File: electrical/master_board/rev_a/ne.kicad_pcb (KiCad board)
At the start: 2 copper layers, 42.2 x 39 mm, 1 part, among them CN60 HCSR04H;F1X4

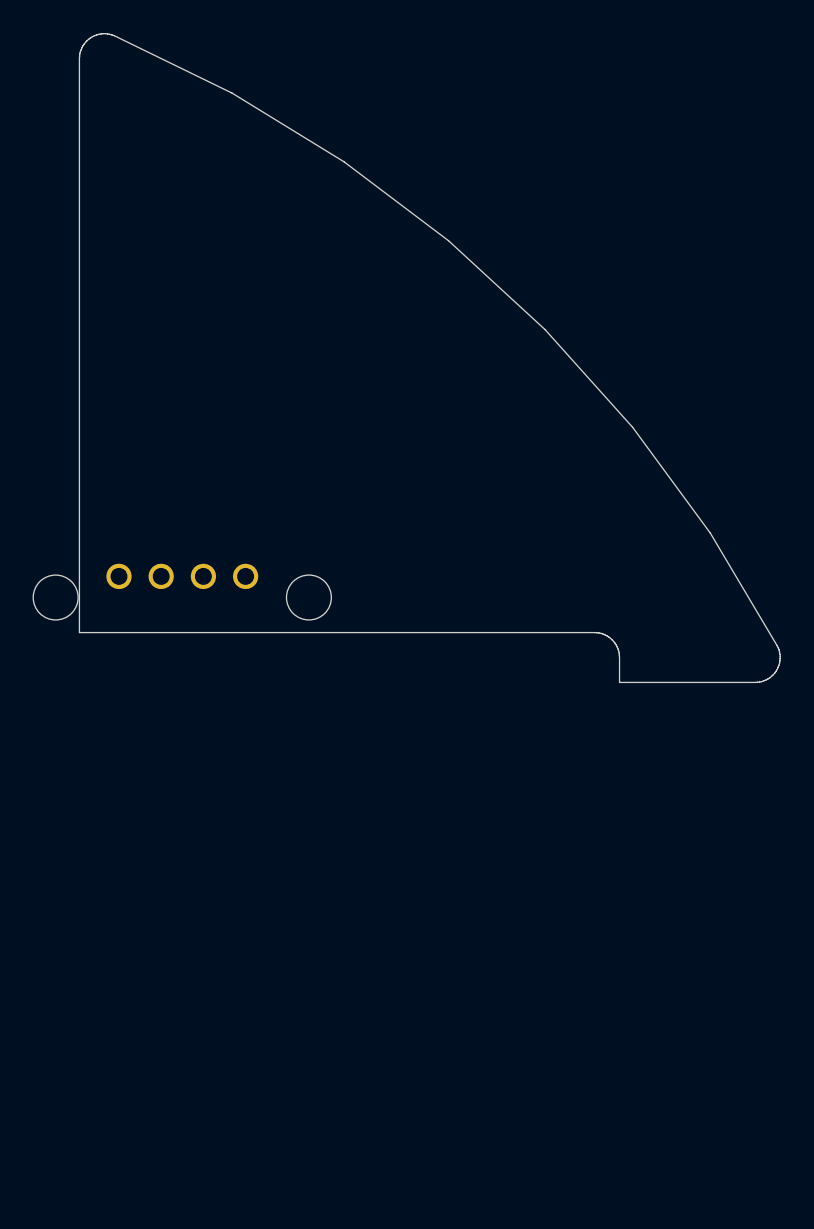
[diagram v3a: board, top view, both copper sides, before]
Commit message: Locked down a minimal version ne.kicad_pcb .
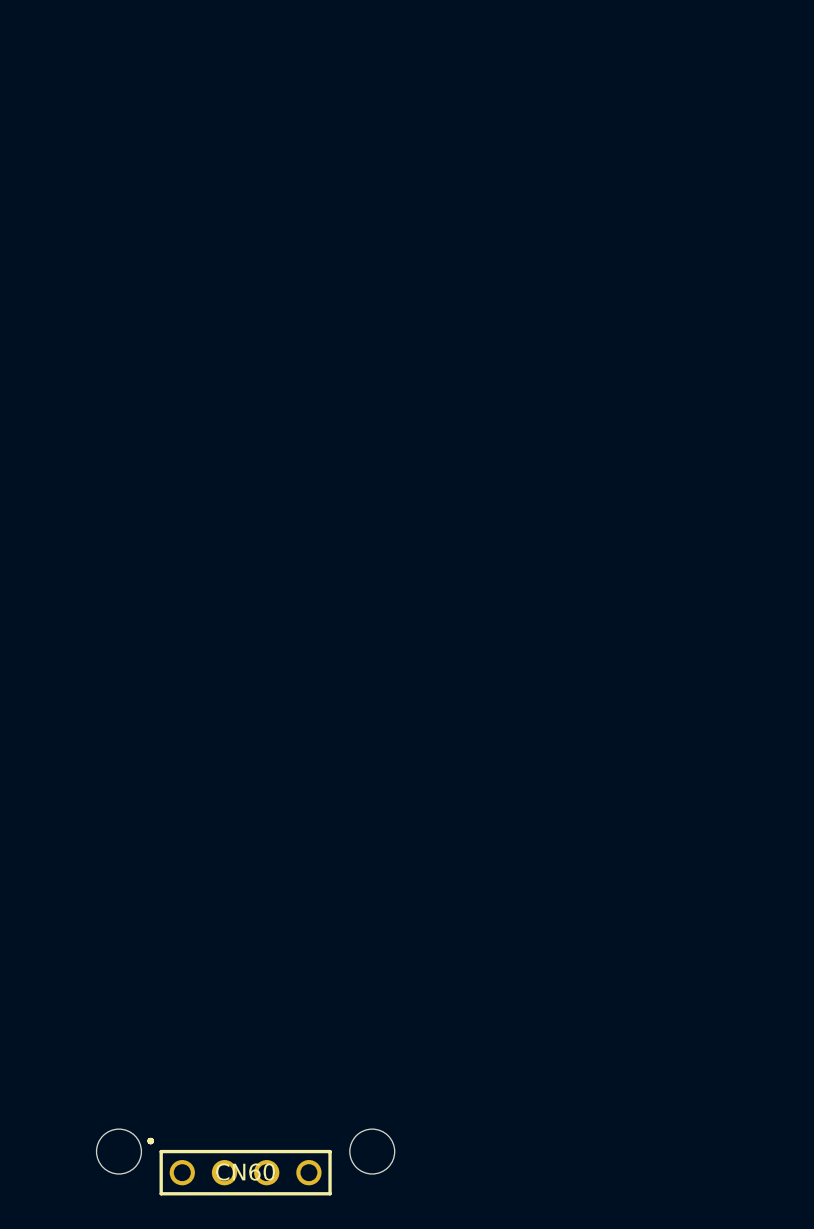
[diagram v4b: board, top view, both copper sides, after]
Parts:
- CN60: moved to F.Cu
- moved CN60 36.1 mm to (140.0, 93.5)
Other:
- board outline removed
- rule pad_to_mask_clearance: 0.05 -> 0

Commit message: Temporary manual version of ne.kicad_pcb for debugging purposes.
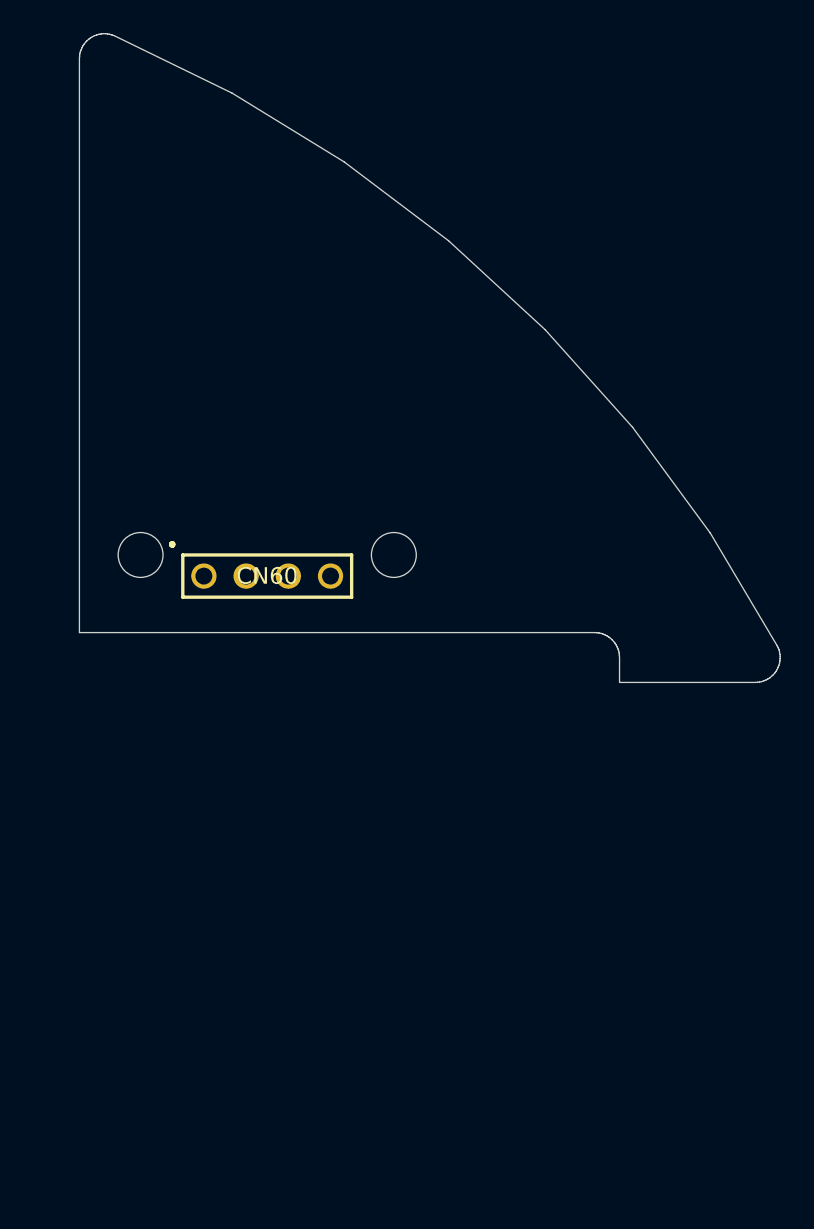
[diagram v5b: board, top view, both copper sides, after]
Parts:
- moved CN60 35.9 mm to (141.3, 57.6)
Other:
- board outline added: 42.2 x 39 mm
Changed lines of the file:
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@@
   (general
     (thickness 1.6)
-    (drawings 0)
+    (drawings 75)
     (tracks 0)
     (zones 0)
@@
   )
   (module HR2:HCSR04_F1x4H_MATE (layer F.Cu)
-    (at 140 93.5)
+    (at 141.3 57.6)
     (fp_text reference CN60 (at 0 0) (layer F.SilkS)
       (effects (font (size 1 1) (thickness 0.2)))
@@
     (pad 1 thru_hole circle (at -3.81 0) (size 1.52 1.52) (drill 1.02) (layers *.Cu *.Mask))
   )
+  (gr_line (start 162.5 64) (end 170.67 64) (layer Edge.Cuts) (width 0.05))
+  (gr_line (start 170.67 64) (end 170.8 63.99) (layer Edge.Cuts) (width 0.05))
+  (gr_line (start 170.8 63.99) (end 170.93 63.98) (layer Edge.Cuts) (width 0.05))
+  (gr_line (start 170.93 63.98) (end 171.06 63.95) (layer Edge.Cuts) (width 0.05))
+  (gr_line (start 171.06 63.95) (end 171.19 63.9) (layer Edge.Cuts) (width 0.05))
+  (gr_line (start 171.19 63.9) (end 171.32 63.85) (layer Edge.Cuts) (width 0.05))
+  (gr_line (start 171.32 63.85) (end 171.43 63.79) (layer Edge.Cuts) (width 0.05))
+  (gr_line (start 171.43 63.79) (end 171.55 63.72) (layer Edge.Cuts) (width 0.05))
+  (gr_line (start 171.55 63.72) (end 171.65 63.63) (layer Edge.Cuts) (width 0.05))
+  (gr_line (start 171.65 63.63) (end 171.75 63.54) (layer Edge.Cuts) (width 0.05))
+  (gr_line (start 171.75 63.54) (end 171.84 63.44) (layer Edge.Cuts) (width 0.05))
+  (gr_line (start 171.84 63.44) (end 171.92 63.33) (layer Edge.Cuts) (width 0.05))
+  (gr_line (start 171.92 63.33) (end 171.99 63.21) (layer Edge.Cuts) (width 0.05))
+  (gr_line (start 171.99 63.21) (end 172.04 63.09) (layer Edge.Cuts) (width 0.05))
+  (gr_line (start 172.04 63.09) (end 172.09 62.97) (layer Edge.Cuts) (width 0.05))
+  (gr_line (start 172.09 62.97) (end 172.13 62.84) (layer Edge.Cuts) (width 0.05))
+  (gr_line (start 172.13 62.84) (end 172.15 62.71) (layer Edge.Cuts) (width 0.05))
+  (gr_line (start 172.15 62.71) (end 172.16 62.57) (layer Edge.Cuts) (width 0.05))
+  (gr_line (start 172.16 62.57) (end 172.17 62.44) (layer Edge.Cuts) (width 0.05))
+  (gr_line (start 172.17 62.44) (end 172.15 62.31) (layer Edge.Cuts) (width 0.05))
+  (gr_line (start 172.15 62.31) (end 172.13 62.17) (layer Edge.Cuts) (width 0.05))
+  (gr_line (start 172.13 62.17) (end 172.1 62.04) (layer Edge.Cuts) (width 0.05))
+  (gr_line (start 172.1 62.04) (end 172.05 61.92) (layer Edge.Cuts) (width 0.05))
+  (gr_line (start 172.05 61.92) (end 171.99 61.8) (layer Edge.Cuts) (width 0.05))
+  (gr_line (start 171.99 61.8) (end 171.99 61.8) (layer Edge.Cuts) (width 0.05))
+  (gr_line (start 171.99 61.8) (end 167.96 55.01) (layer Edge.Cuts) (width 0.05))
+  (gr_line (start 167.96 55.01) (end 163.29 48.65) (layer Edge.Cuts) (width 0.05))
+  (gr_line (start 163.29 48.65) (end 158.02 42.77) (layer Edge.Cuts) (width 0.05))
+  (gr_line (start 158.02 42.77) (end 152.21 37.42) (layer Edge.Cuts) (width 0.05))
+  (gr_line (start 152.21 37.42) (end 145.92 32.67) (layer Edge.Cuts) (width 0.05))
+  (gr_line (start 145.92 32.67) (end 139.19 28.54) (layer Edge.Cuts) (width 0.05))
+  (gr_line (start 139.19 28.54) (end 132.09 25.08) (layer Edge.Cuts) (width 0.05))
+  (gr_line (start 132.09 25.08) (end 131.96 25.04) (layer Edge.Cuts) (width 0.05))
+  (gr_line (start 131.96 25.04) (end 131.83 25) (layer Edge.Cuts) (width 0.05))
+  (gr_line (start 131.83 25) (end 131.7 24.98) (layer Edge.Cuts) (width 0.05))
+  (gr_line (start 131.7 24.98) (end 131.57 24.96) (layer Edge.Cuts) (width 0.05))
+  (gr_line (start 131.57 24.96) (end 131.43 24.96) (layer Edge.Cuts) (width 0.05))
+  (gr_line (start 131.43 24.96) (end 131.3 24.98) (layer Edge.Cuts) (width 0.05))
+  (gr_line (start 131.3 24.98) (end 131.17 25) (layer Edge.Cuts) (width 0.05))
+  (gr_line (start 131.17 25) (end 131.04 25.04) (layer Edge.Cuts) (width 0.05))
+  (gr_line (start 131.04 25.04) (end 130.91 25.08) (layer Edge.Cuts) (width 0.05))
+  (gr_line (start 130.91 25.08) (end 130.79 25.14) (layer Edge.Cuts) (width 0.05))
+  (gr_line (start 130.79 25.14) (end 130.67 25.21) (layer Edge.Cuts) (width 0.05))
+  (gr_line (start 130.67 25.21) (end 130.57 25.29) (layer Edge.Cuts) (width 0.05))
+  (gr_line (start 130.57 25.29) (end 130.46 25.38) (layer Edge.Cuts) (width 0.05))
+  (gr_line (start 130.46 25.38) (end 130.37 25.48) (layer Edge.Cuts) (width 0.05))
+  (gr_line (start 130.37 25.48) (end 130.29 25.58) (layer Edge.Cuts) (width 0.05))
+  (gr_line (start 130.29 25.58) (end 130.21 25.69) (layer Edge.Cuts) (width 0.05))
+  (gr_line (start 130.21 25.69) (end 130.15 25.81) (layer Edge.Cuts) (width 0.05))
+  (gr_line (start 130.15 25.81) (end 130.1 25.94) (layer Edge.Cuts) (width 0.05))
+  (gr_line (start 130.1 25.94) (end 130.05 26.06) (layer Edge.Cuts) (width 0.05))
+  (gr_line (start 130.05 26.06) (end 130.02 26.19) (layer Edge.Cuts) (width 0.05))
+  (gr_line (start 130.02 26.19) (end 130.01 26.33) (layer Edge.Cuts) (width 0.05))
+  (gr_line (start 130.01 26.33) (end 130 26.46) (layer Edge.Cuts) (width 0.05))
+  (gr_line (start 130 26.46) (end 130 61) (layer Edge.Cuts) (width 0.05))
+  (gr_line (start 130 61) (end 161 61) (layer Edge.Cuts) (width 0.05))
+  (gr_line (start 161 61) (end 161.13 61.01) (layer Edge.Cuts) (width 0.05))
+  (gr_line (start 161.13 61.01) (end 161.26 61.02) (layer Edge.Cuts) (width 0.05))
+  (gr_line (start 161.26 61.02) (end 161.39 61.05) (layer Edge.Cuts) (width 0.05))
+  (gr_line (start 161.39 61.05) (end 161.51 61.09) (layer Edge.Cuts) (width 0.05))
+  (gr_line (start 161.51 61.09) (end 161.63 61.14) (layer Edge.Cuts) (width 0.05))
+  (gr_line (start 161.63 61.14) (end 161.75 61.2) (layer Edge.Cuts) (width 0.05))
+  (gr_line (start 161.75 61.2) (end 161.86 61.27) (layer Edge.Cuts) (width 0.05))
+  (gr_line (start 161.86 61.27) (end 161.96 61.35) (layer Edge.Cuts) (width 0.05))
+  (gr_line (start 161.96 61.35) (end 162.06 61.44) (layer Edge.Cuts) (width 0.05))
+  (gr_line (start 162.06 61.44) (end 162.15 61.54) (layer Edge.Cuts) (width 0.05))
+  (gr_line (start 162.15 61.54) (end 162.23 61.64) (layer Edge.Cuts) (width 0.05))
+  (gr_line (start 162.23 61.64) (end 162.3 61.75) (layer Edge.Cuts) (width 0.05))
+  (gr_line (start 162.3 61.75) (end 162.36 61.87) (layer Edge.Cuts) (width 0.05))
+  (gr_line (start 162.36 61.87) (end 162.41 61.99) (layer Edge.Cuts) (width 0.05))
+  (gr_line (start 162.41 61.99) (end 162.45 62.11) (layer Edge.Cuts) (width 0.05))
+  (gr_line (start 162.45 62.11) (end 162.48 62.24) (layer Edge.Cuts) (width 0.05))
+  (gr_line (start 162.48 62.24) (end 162.49 62.37) (layer Edge.Cuts) (width 0.05))
+  (gr_line (start 162.49 62.37) (end 162.5 62.5) (layer Edge.Cuts) (width 0.05))
+  (gr_line (start 162.5 62.5) (end 162.5 64) (layer Edge.Cuts) (width 0.05))
 )

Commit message: Another manually generate ne.kicad_pcb for debugging purposes.
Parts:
- CN60: value HCSR04H;F1X4 -> HCSR04;F1X4H; footprint HR2:HCSR04_F1x4H_MATE -> HR2:HCSR04_F1x4H
- moved CN60 2.34 mm to (139.1, 58.4)
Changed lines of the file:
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@@
     (add_net "Net-(CN60-Pad4)")
   )
-  (module HR2:HCSR04_F1x4H_MATE (layer F.Cu)
-    (at 141.3 57.6)
-    (fp_text reference CN60 (at 0 0) (layer F.SilkS)
+  (module HR2:HCSR04_F1x4H (layer F.Cu)
+    (at 139.1 58.4)
+    (fp_text reference CN60 (at 0 -2) (layer F.SilkS)
       (effects (font (size 1 1) (thickness 0.2)))
     )
-    (fp_text value HCSR04H;F1X4 (at 0 -2) (layer F.Fab)
+    (fp_text value HCSR04;F1X4H (at 0 0) (layer F.Fab)
       (effects (font (size 1 1) (thickness 0.2)))
     )
@@
     (fp_line (start -5.08 1.27) (end -5.08 -1.27) (layer F.SilkS) (width 0.2))
     (fp_line (start -5.08 -1.27) (end 5.08 -1.27) (layer F.SilkS) (width 0.2))
-    (fp_line (start -5.62 -1.91) (end -5.64 -1.98) (layer F.SilkS) (width 0.2))
-    (fp_line (start -5.64 -1.98) (end -5.71 -2) (layer F.SilkS) (width 0.2))
-    (fp_line (start -5.71 -2) (end -5.79 -1.98) (layer F.SilkS) (width 0.2))
-    (fp_line (start -5.79 -1.98) (end -5.81 -1.91) (layer F.SilkS) (width 0.2))
-    (fp_line (start -5.81 -1.91) (end -5.79 -1.83) (layer F.SilkS) (width 0.2))
-    (fp_line (start -5.79 -1.83) (end -5.71 -1.8) (layer F.SilkS) (width 0.2))
-    (fp_line (start -5.71 -1.8) (end -5.64 -1.83) (layer F.SilkS) (width 0.2))
-    (fp_line (start -5.64 -1.83) (end -5.62 -1.91) (layer F.SilkS) (width 0.2))
-    (pad "HCSR04 West Tie Down Hole" np_thru_hole circle (at -7.62 -1.27) (size 2.7 2.7) (drill 2.7) (layers *.Cu *.Mask))
-    (pad "HCSR04 East Tie Down Hole" np_thru_hole circle (at 7.62 -1.27) (size 2.7 2.7) (drill 2.7) (layers *.Cu *.Mask))
-    (pad 4 thru_hole circle (at 3.81 0) (size 1.52 1.52) (drill 1.02) (layers *.Cu *.Mask))
-    (pad 3 thru_hole circle (at 1.27 0) (size 1.52 1.52) (drill 1.02) (layers *.Cu *.Mask))
-    (pad 2 thru_hole circle (at -1.27 0) (size 1.52 1.52) (drill 1.02) (layers *.Cu *.Mask))
-    (pad 1 thru_hole circle (at -3.81 0) (size 1.52 1.52) (drill 1.02) (layers *.Cu *.Mask))
+    (fp_line (start 5.18 -1.91) (end 5.15 -1.98) (layer F.SilkS) (width 0.2))
+    (fp_line (start 5.15 -1.98) (end 5.08 -2) (layer F.SilkS) (width 0.2))
+    (fp_line (start 5.08 -2) (end 5.01 -1.98) (layer F.SilkS) (width 0.2))
+    (fp_line (start 5.01 -1.98) (end 4.98 -1.91) (layer F.SilkS) (width 0.2))
+    (fp_line (start 4.98 -1.91) (end 5.01 -1.83) (layer F.SilkS) (width 0.2))
+    (fp_line (start 5.01 -1.83) (end 5.08 -1.8) (layer F.SilkS) (width 0.2))
+    (fp_line (start 5.08 -1.8) (end 5.15 -1.83) (layer F.SilkS) (width 0.2))
+    (fp_line (start 5.15 -1.83) (end 5.18 -1.91) (layer F.SilkS) (width 0.2))
+    (pad "HCSR04 West Tie Down Hole" np_thru_hole circle (at -6.555 -1.27) (size 2.55 2.55) (drill 2.55) (layers *.Cu *.Mask))
+    (pad "HCSR04 East Tie Down Hole" np_thru_hole circle (at 6.555 -1.27) (size 2.55 2.55) (drill 2.55) (layers *.Cu *.Mask))
+    (pad 4 thru_hole circle (at -3.81 0) (size 1.52 1.52) (drill 1.02) (layers *.Cu *.Mask))
+    (pad 3 thru_hole circle (at -1.27 0) (size 1.52 1.52) (drill 1.02) (layers *.Cu *.Mask))
+    (pad 2 thru_hole circle (at 1.27 0) (size 1.52 1.52) (drill 1.02) (layers *.Cu *.Mask))
+    (pad 1 thru_hole circle (at 3.81 0) (size 1.52 1.52) (drill 1.02) (layers *.Cu *.Mask))
   )
   (gr_line (start 162.5 64) (end 170.67 64) (layer Edge.Cuts) (width 0.05))

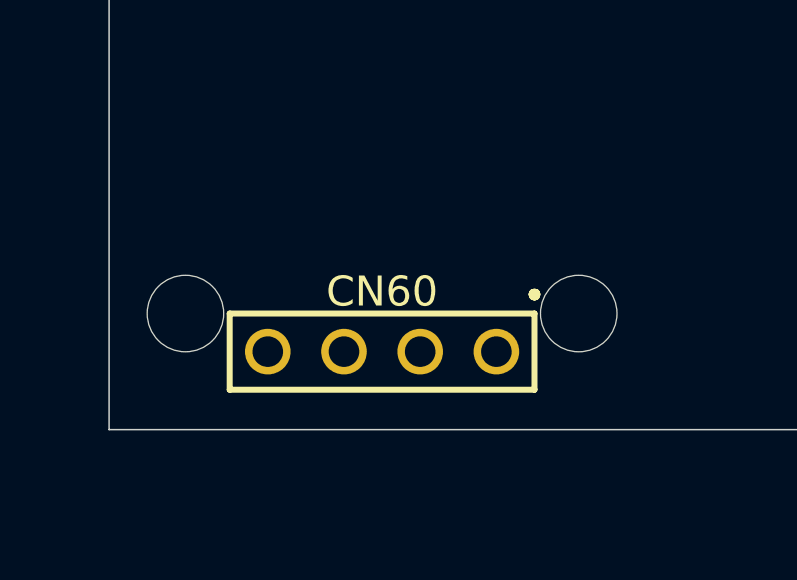
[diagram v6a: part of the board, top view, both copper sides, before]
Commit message: Successfully placed a font surface non-rotated footprint in ne.kicad_pcb.
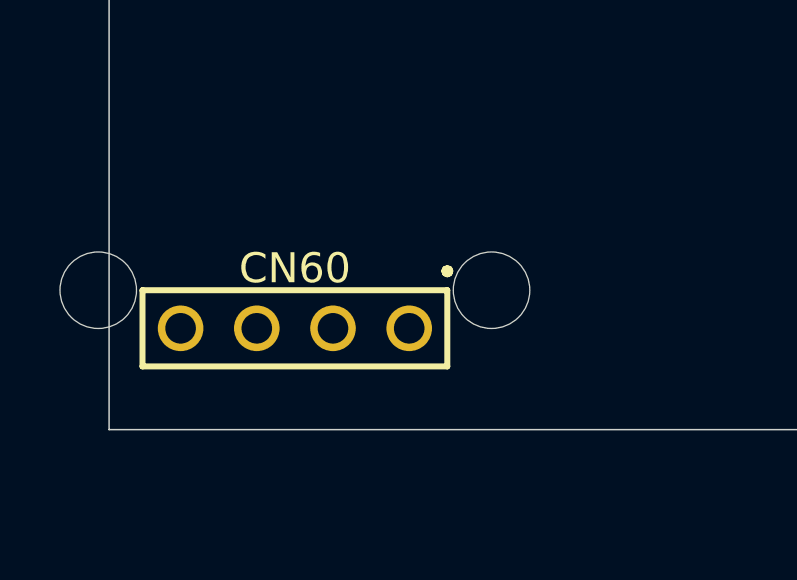
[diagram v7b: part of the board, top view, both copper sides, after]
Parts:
- CN60: value HCSR04;F1X4H -> HCSR04;F1x4H
- moved CN60 3.01 mm to (136.2, 57.6)
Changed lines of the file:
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@@
   )
   (module HR2:HCSR04_F1x4H (layer F.Cu)
-    (at 139.1 58.4)
+    (at 136.1937 57.6226)
     (fp_text reference CN60 (at 0 -2) (layer F.SilkS)
       (effects (font (size 1 1) (thickness 0.2)))
     )
-    (fp_text value HCSR04;F1X4H (at 0 0) (layer F.Fab)
+    (fp_text value HCSR04;F1x4H (at 0 0) (layer F.Fab)
       (effects (font (size 1 1) (thickness 0.2)))
     )
